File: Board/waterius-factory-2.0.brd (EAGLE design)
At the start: 13.5 x 51 mm, 24 parts, among them IC1 TINY13-20SU, U3 ESP01

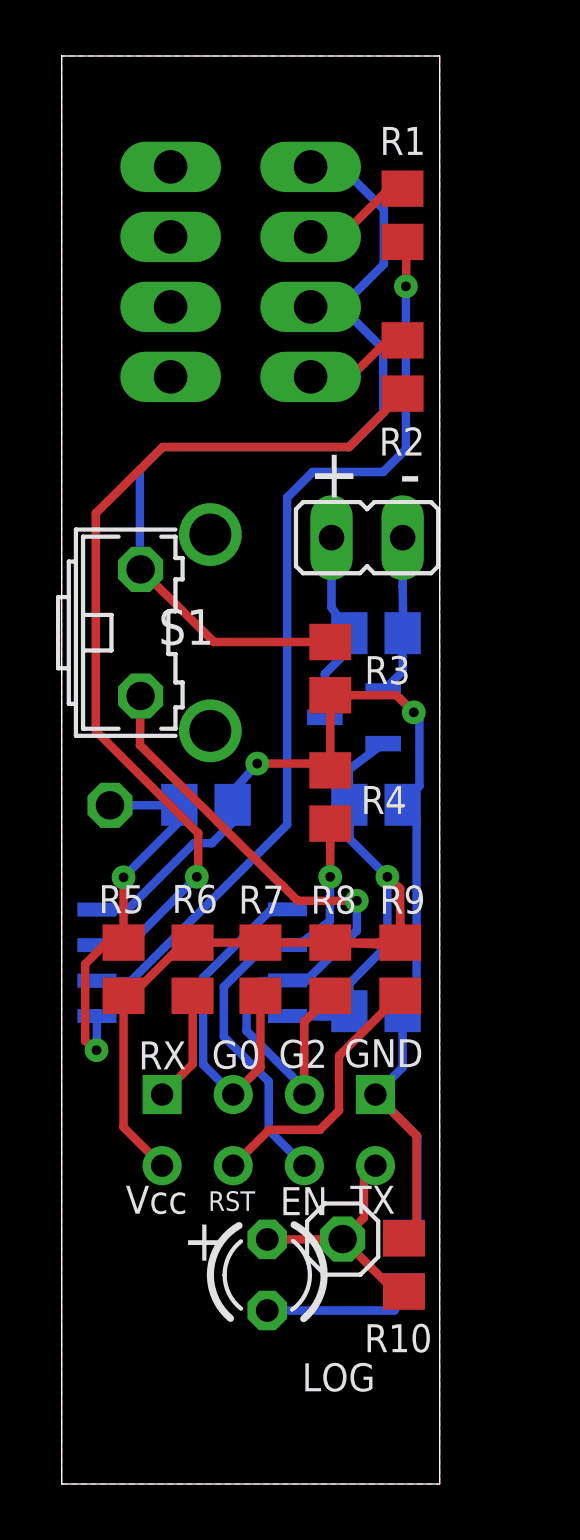
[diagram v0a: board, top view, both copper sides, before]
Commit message: correct Board 2.0
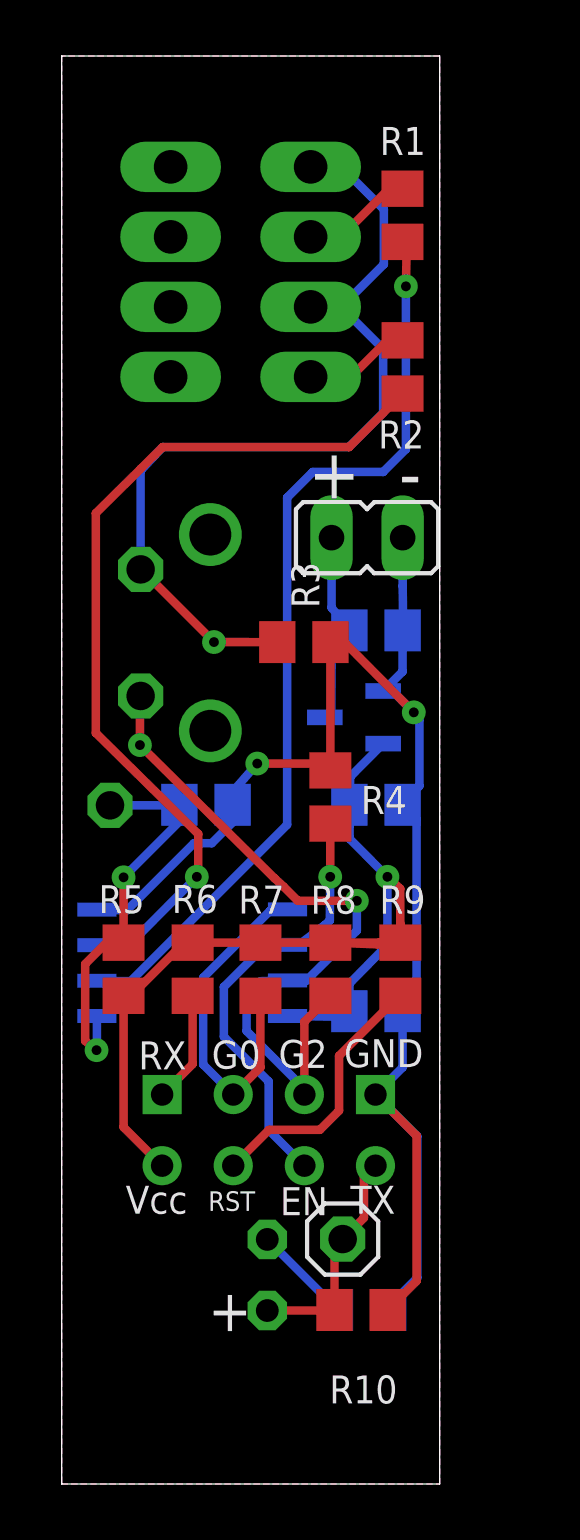
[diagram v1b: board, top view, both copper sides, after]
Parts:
- moved R11 2.22 mm to (10.7, 6.21), turned to 0 degrees
- moved R10 2.22 mm to (10.7, 6.21), turned to 180 degrees
- moved R3 1.34 mm to (8.65, 30.1), turned to 0 degrees
- moved C1 0.10 mm to (11.2, 30.5)
- flipped LED1 to the bottom, turned to 90 degrees
- flipped S1 to the bottom, turned to 90 degrees
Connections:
- net GND1: now also S1.2; no longer S1.1
- net SCK: now also S1.1; no longer S1.2
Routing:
- net GND: track 51.1 -> 59.5 mm
- net N$6: track 5.45 -> 3.52 mm
- net GND1: track 33.8 -> 31.9 mm, vias 0 -> 1
- net N$5: track 8.77 -> 8.17 mm
- net SCK: track 26.0 -> 26.1 mm, vias 1 -> 2

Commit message: board correct, https://github.com/dontsovcmc/waterius/issues/87
remove 47k untested resister
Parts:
- removed R10: 47к, resistor:R0805
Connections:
- net GND: no longer R10.1
- net N$5: no longer R10.2
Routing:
- net GND: track 59.5 -> 50.8 mm
- net N$5: track 8.17 -> 7.27 mm
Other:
- board text added: "- +"
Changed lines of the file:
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@@
 <?xml version="1.0" encoding="utf-8"?>
 <!DOCTYPE eagle SYSTEM "eagle.dtd">
-<eagle version="9.0.1">
+<eagle version="9.0.0">
 <drawing>
 <settings>
@@
 <layer number="16" name="Bottom" color="1" fill="1" visible="yes" active="yes"/>
 <layer number="17" name="Pads" color="2" fill="1" visible="yes" active="yes"/>
-<layer number="18" name="Vias" color="2" fill="1" visible="yes" active="yes"/>
+<layer number="18" name="Vias" color="2" fill="1" visible="no" active="yes"/>
 <layer number="19" name="Unrouted" color="6" fill="1" visible="yes" active="yes"/>
-<layer number="20" name="Dimension" color="24" fill="1" visible="yes" active="yes"/>
-<layer number="21" name="tPlace" color="7" fill="1" visible="yes" active="yes"/>
-<layer number="22" name="bPlace" color="7" fill="1" visible="yes" active="yes"/>
+<layer number="20" name="Dimension" color="24" fill="1" visible="no" active="yes"/>
+<layer number="21" name="tPlace" color="7" fill="1" visible="no" active="yes"/>
+<layer number="22" name="bPlace" color="7" fill="1" visible="no" active="yes"/>
 <layer number="23" name="tOrigins" color="15" fill="1" visible="yes" active="yes"/>
 <layer number="24" name="bOrigins" color="15" fill="1" visible="yes" active="yes"/>
 <layer number="25" name="tNames" color="7" fill="1" visible="yes" active="yes"/>
-<layer number="26" name="bNames" color="7" fill="1" visible="yes" active="yes"/>
+<layer number="26" name="bNames" color="7" fill="1" visible="no" active="yes"/>
 <layer number="27" name="tValues" color="7" fill="1" visible="no" active="yes"/>
 <layer number="28" name="bValues" color="7" fill="1" visible="no" active="yes"/>
@@
 <layer number="37" name="tTest" color="7" fill="1" visible="no" active="yes"/>
 <layer number="38" name="bTest" color="7" fill="1" visible="no" active="yes"/>
-<layer number="39" name="tKeepout" color="4" fill="11" visible="no" active="yes"/>
-<layer number="40" name="bKeepout" color="1" fill="11" visible="yes" active="yes"/>
-<layer number="41" name="tRestrict" color="4" fill="10" visible="no" active="yes"/>
-<layer number="42" name="bRestrict" color="1" fill="10" visible="yes" active="yes"/>
+<layer number="39" name="tKeepout" color="4" fill="11" visible="yes" active="yes"/>
+<layer number="40" name="bKeepout" color="1" fill="11" visible="no" active="yes"/>
+<layer number="41" name="tRestrict" color="4" fill="10" visible="yes" active="yes"/>
+<layer number="42" name="bRestrict" color="1" fill="10" visible="no" active="yes"/>
 <layer number="43" name="vRestrict" color="2" fill="10" visible="no" active="yes"/>
 <layer number="44" name="Drills" color="7" fill="1" visible="no" active="yes"/>
@@
 <layer number="48" name="Document" color="7" fill="1" visible="no" active="yes"/>
 <layer number="49" name="Reference" color="7" fill="1" visible="no" active="yes"/>
-<layer number="51" name="tDocu" color="7" fill="1" visible="no" active="yes"/>
-<layer number="52" name="bDocu" color="7" fill="1" visible="yes" active="yes"/>
+<layer number="51" name="tDocu" color="7" fill="1" visible="yes" active="yes"/>
+<layer number="52" name="bDocu" color="7" fill="1" visible="no" active="yes"/>
 <layer number="88" name="SimResults" color="9" fill="1" visible="no" active="no"/>
 <layer number="89" name="SimProbes" color="9" fill="1" visible="no" active="no"/>
@@
 <dimension x1="0" y1="0" x2="0" y2="7.5" x3="-10.774365625" y3="3.75" textsize="1.778" layer="47"/>
 <dimension x1="0" y1="0" x2="0" y2="30.5" x3="-15.66665" y3="15.25" textsize="1.778" layer="47"/>
-<text x="12.827" y="35.2806" size="1.778" layer="26" rot="MR0">+  -</text>
+<text x="12.9286" y="35.3314" size="1.778" layer="26" rot="MR0">-   +</text>
 <dimension x1="-1.8542" y1="35.4584" x2="-1.8542" y2="39.4208" x3="-2.7686" y3="37.4396" textsize="1.778" layer="1"/>
 <dimension x1="0" y1="52" x2="3.0226" y2="51.9684" x3="1.5338625" y3="54.1427" textsize="1.778" layer="1"/>
@@
 <attribute name="SUPPLIER" value="Microchip" x="10.4394" y="27.3812" size="0.5" layer="28" rot="MR270" display="off"/>
 </element>
-<element name="R10" library="resistor" package="R0805" value="47к" x="10.6934" y="6.215" smashed="yes" rot="R180">
-<attribute name="NAME" x="11.9888" y="3.8782" size="1" layer="25" rot="R180"/>
-</element>
 <element name="S1" library="switch-omron" library_urn="urn:adsk.eagle:library:377" package="B3F-31XX" package3d_urn="urn:adsk.eagle:package:27487/1" value="" x="4.064" y="30.4038" smashed="yes" rot="MR90">
 <attribute name="MF" value="" x="4.064" y="30.4038" size="1.778" layer="28" rot="MR90" display="off"/>
@@
 <contactref element="C3" pad="2"/>
 <contactref element="U$1" pad="1"/>
-<contactref element="R10" pad="1"/>
 <wire x1="11.2119" y1="13.9087" x2="11.2066" y2="13.9087" width="0.3048" layer="16"/>
 <wire x1="11.2119" y1="13.9087" x2="11.2066" y2="13.9087" width="0.3048" layer="1"/>
-<wire x1="11.2066" y1="13.9087" x2="12.6746" y2="12.4407" width="0.3048" layer="1"/>
-<wire x1="12.6746" y1="7.2492" x2="11.6434" y2="6.215" width="0.3048" layer="1"/>
-<wire x1="12.6746" y1="12.4407" x2="12.6746" y2="7.2492" width="0.3048" layer="1"/>
-<wire x1="11.2066" y1="13.9087" x2="12.7" y2="12.4153" width="0.3048" layer="16"/>
-<wire x1="12.7" y1="12.4153" x2="12.7" y2="7.366" width="0.3048" layer="16"/>
+<wire x1="12.7" y1="7.366" x2="12.7" y2="12.4153" width="0.3048" layer="16"/>
 <wire x1="1.2574" y1="20.5134" x2="2.327" y2="20.488" width="0.3048" layer="16"/>
 <wire x1="2.327" y1="20.488" x2="4.7244" y2="22.8854" width="0.3048" layer="16"/>
@@
 <wire x1="12.7" y1="7.366" x2="11.6586" y2="6.3246" width="0.3048" layer="16"/>
 <wire x1="11.6586" y1="6.3246" x2="11.6586" y2="6.215" width="0.3048" layer="16"/>
+<wire x1="12.7" y1="12.4153" x2="11.2066" y2="13.9087" width="0.3048" layer="16"/>
 </signal>
 <signal name="IN2">
@@
 <contactref element="LOG" pad="1"/>
 <contactref element="LED1" pad="A"/>
-<contactref element="R10" pad="2"/>
 <wire x1="10.0348" y1="8.7476" x2="10.795" y2="9.5078" width="0.3048" layer="1"/>
 <wire x1="10.795" y1="10.9571" x2="11.2066" y2="11.3687" width="0.3048" layer="1"/>
 <wire x1="10.795" y1="9.5078" x2="10.795" y2="10.9571" width="0.3048" layer="1"/>
-<wire x1="9.7434" y1="6.215" x2="9.7238" y2="6.1954" width="0.3048" layer="1"/>
-<wire x1="9.7238" y1="6.1954" x2="7.3424" y2="6.1954" width="0.3048" layer="1"/>
 <wire x1="10.0348" y1="8.7476" x2="9.7434" y2="8.4562" width="0.3048" layer="1"/>
-<wire x1="9.7434" y1="8.4562" x2="9.7434" y2="6.215" width="0.3048" layer="1"/>
+<wire x1="10.0348" y1="8.7476" x2="7.4826" y2="6.1954" width="0.3048" layer="1"/>
+<wire x1="7.4826" y1="6.1954" x2="7.3424" y2="6.1954" width="0.3048" layer="1"/>
 </signal>
 <signal name="N$6">
@@
 </signal>
 </signals>
+<errors>
+</errors>
 </board>
 </drawing>

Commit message: board
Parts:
- turned LED1 to 270 degrees
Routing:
- net N$6: track 3.52 -> 2.42 mm
- net N$5: track 7.27 -> 6.21 mm
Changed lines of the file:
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@@
 <?xml version="1.0" encoding="utf-8"?>
 <!DOCTYPE eagle SYSTEM "eagle.dtd">
-<eagle version="9.0.0">
+<eagle version="9.0.1">
 <drawing>
 <settings>
@@
 <text x="12.2428" y="1.3" size="1" layer="26" rot="MR0">TX</text>
 <text x="1.8542" y="10.9982" size="1" layer="26" rot="MR270">waterius.ru</text>
-<text x="5.2324" y="5.461" size="1.5" layer="25">+</text>
+<text x="5.1562" y="8.001" size="1.5" layer="25">+</text>
 <dimension x1="0" y1="0" x2="0" y2="7.5" x3="-10.774365625" y3="3.75" textsize="1.778" layer="47"/>
 <dimension x1="0" y1="0" x2="0" y2="30.5" x3="-15.66665" y3="15.25" textsize="1.778" layer="47"/>
 <text x="12.9286" y="35.3314" size="1.778" layer="26" rot="MR0">-   +</text>
-<dimension x1="-1.8542" y1="35.4584" x2="-1.8542" y2="39.4208" x3="-2.7686" y3="37.4396" textsize="1.778" layer="1"/>
 <dimension x1="0" y1="52" x2="3.0226" y2="51.9684" x3="1.5338625" y3="54.1427" textsize="1.778" layer="1"/>
 <dimension x1="0" y1="0" x2="-0.0508" y2="39.5224" x3="-11.58323125" y3="19.74634375" textsize="1.778" layer="1"/>
@@
 </element>
 <element name="U3" library="esp8266modules" package="ESP01" value="ESP01" x="7.3816" y="19.5462" smashed="yes" rot="MR0"/>
-<element name="LED1" library="led" package="LED3MM" value="RED" x="7.3424" y="7.4654" smashed="yes" rot="MR90"/>
+<element name="LED1" library="led" package="LED3MM" value="RED" x="7.3424" y="7.4654" smashed="yes" rot="MR270"/>
 <element name="R11" library="resistor" package="R0805" value="300" x="10.7086" y="6.215" smashed="yes" rot="MR0">
 <attribute name="NAME" x="11.86" y="4.2732" size="1" layer="26" rot="MR0"/>
@@
 <wire x1="10.795" y1="9.5078" x2="10.795" y2="10.9571" width="0.3048" layer="1"/>
 <wire x1="10.0348" y1="8.7476" x2="9.7434" y2="8.4562" width="0.3048" layer="1"/>
-<wire x1="10.0348" y1="8.7476" x2="7.4826" y2="6.1954" width="0.3048" layer="1"/>
-<wire x1="7.4826" y1="6.1954" x2="7.3424" y2="6.1954" width="0.3048" layer="1"/>
+<wire x1="10.0348" y1="8.7476" x2="7.381" y2="8.7354" width="0.3048" layer="1"/>
+<wire x1="7.381" y1="8.7354" x2="7.3424" y2="8.7354" width="0.3048" layer="1"/>
 </signal>
 <signal name="N$6">
 <contactref element="R11" pad="2"/>
 <contactref element="LED1" pad="K"/>
-<wire x1="7.3424" y1="8.7354" x2="9.7586" y2="6.3192" width="0.3048" layer="16"/>
-<wire x1="9.7586" y1="6.3192" x2="9.7586" y2="6.215" width="0.3048" layer="16"/>
+<wire x1="7.3424" y1="6.1954" x2="9.6062" y2="6.1922" width="0.3048" layer="16"/>
+<wire x1="9.6062" y1="6.1922" x2="9.7586" y2="6.215" width="0.3048" layer="16"/>
 </signal>
 <signal name="N$4">

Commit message: replace mcp1700 file
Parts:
- U$1: device Microchip_By_element14_Batch_1:SOT95P237X112-3N -> MCP1700T-3002E_TT:SOT95P237X112-3N
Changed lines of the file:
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@@
 <?xml version="1.0" encoding="utf-8"?>
 <!DOCTYPE eagle SYSTEM "eagle.dtd">
-<eagle version="9.0.1">
+<eagle version="9.0.0">
 <drawing>
 <settings>
@@
 <attribute name="SPICEPREFIX" value="C" x="5.1538" y="24.2566" size="1.778" layer="28" rot="MR180" display="off"/>
 </element>
-<element name="U$1" library="Microchip_By_element14_Batch_1" package="SOT95P237X112-3N" value="MCP1700T-3002E/TT" x="10.4394" y="27.3812" smashed="yes" rot="MR270">
-<attribute name="MPN" value="MCP1700T-3002E/TT" x="10.4394" y="27.3812" size="0.5" layer="28" rot="MR270" display="off"/>
-<attribute name="OC_FARNELL" value="1331482" x="10.4394" y="27.3812" size="0.5" layer="28" rot="MR270" display="off"/>
-<attribute name="OC_NEWARK" value="84R5176" x="10.4394" y="27.3812" size="0.5" layer="28" rot="MR270" display="off"/>
-<attribute name="PACKAGE" value="SOT23-3" x="10.4394" y="27.3812" size="0.5" layer="28" rot="MR270" display="off"/>
-<attribute name="SUPPLIER" value="Microchip" x="10.4394" y="27.3812" size="0.5" layer="28" rot="MR270" display="off"/>
+<element name="U$1" library="MCP1700T-3002E_TT" package="SOT95P237X112-3N" value="MCP1700T-3002E/TT" x="10.4394" y="27.3812" smashed="yes" rot="MR270">
+<attribute name="AVAILABILITY" value="Unavailable" x="10.4394" y="27.3812" size="1.778" layer="28" rot="MR270" display="off"/>
+<attribute name="DESCRIPTION" value=" MCP1700 Series 250 mA 3 V Fixed Output LDO Voltage Regulator - SOT-23 " x="10.4394" y="27.3812" size="1.778" layer="28" rot="MR270" display="off"/>
+<attribute name="MF" value="Microchip" x="10.4394" y="27.3812" size="1.778" layer="28" rot="MR270" display="off"/>
+<attribute name="MP" value="MCP1700T-3002E/TT" x="10.4394" y="27.3812" size="1.778" layer="28" rot="MR270" display="off"/>
+<attribute name="PACKAGE" value="SOT-23 Microchip" x="10.4394" y="27.3812" size="0.5" layer="28" rot="MR270" display="off"/>
+<attribute name="PRICE" value="None" x="10.4394" y="27.3812" size="1.778" layer="28" rot="MR270" display="off"/>
 </element>
 <element name="S1" library="switch-omron" library_urn="urn:adsk.eagle:library:377" package="B3F-31XX" package3d_urn="urn:adsk.eagle:package:27487/1" value="" x="4.064" y="30.4038" smashed="yes" rot="MR90">

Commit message: attiny85 on sch
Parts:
- IC1: value TINY13-20SU -> TINY85-20SU
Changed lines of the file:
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@@
 <?xml version="1.0" encoding="utf-8"?>
 <!DOCTYPE eagle SYSTEM "eagle.dtd">
-<eagle version="9.0.0">
+<eagle version="9.0.1">
 <drawing>
 <settings>
@@
 <attribute name="NAME" x="2.9702" y="25.6092" size="1" layer="26" ratio="10" rot="MR0"/>
 </element>
-<element name="IC1" library="atmel" package="8S2" value="TINY13-20SU" x="4.6614" y="18.6184" smashed="yes" rot="MR90">
+<element name="IC1" library="atmel" package="8S2" value="TINY85-20SU" x="4.6614" y="18.6184" smashed="yes" rot="MR90">
 <attribute name="MF" value="" x="4.6614" y="18.6184" size="1.778" layer="28" rot="MR90" display="off"/>
 <attribute name="MPN" value="ATTINY13-20SU" x="4.6614" y="18.6184" size="1.778" layer="28" rot="MR90" display="off"/>
